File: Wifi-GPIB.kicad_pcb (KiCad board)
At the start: 2 copper layers, 63 x 100.6 mm, 61 parts, among them CON1 POWER_BARREL, P1 CONN_6, P2 CONN_2, P3 CONN_8, P4 GPIB_MALE, P5 CONN_4, Q1 IRLML2246TR, SW1 SW_RESET, SW2 SW_BOOTL, U1 MICRO-B_USB, U2 AP1117E50G-13, U3 LM358, U4 BA33BC0FP-E2, U5 STM32F072CBT6, U6 SN75160B, U7 SN75162B, U8 ESP-12/07v2/08v2

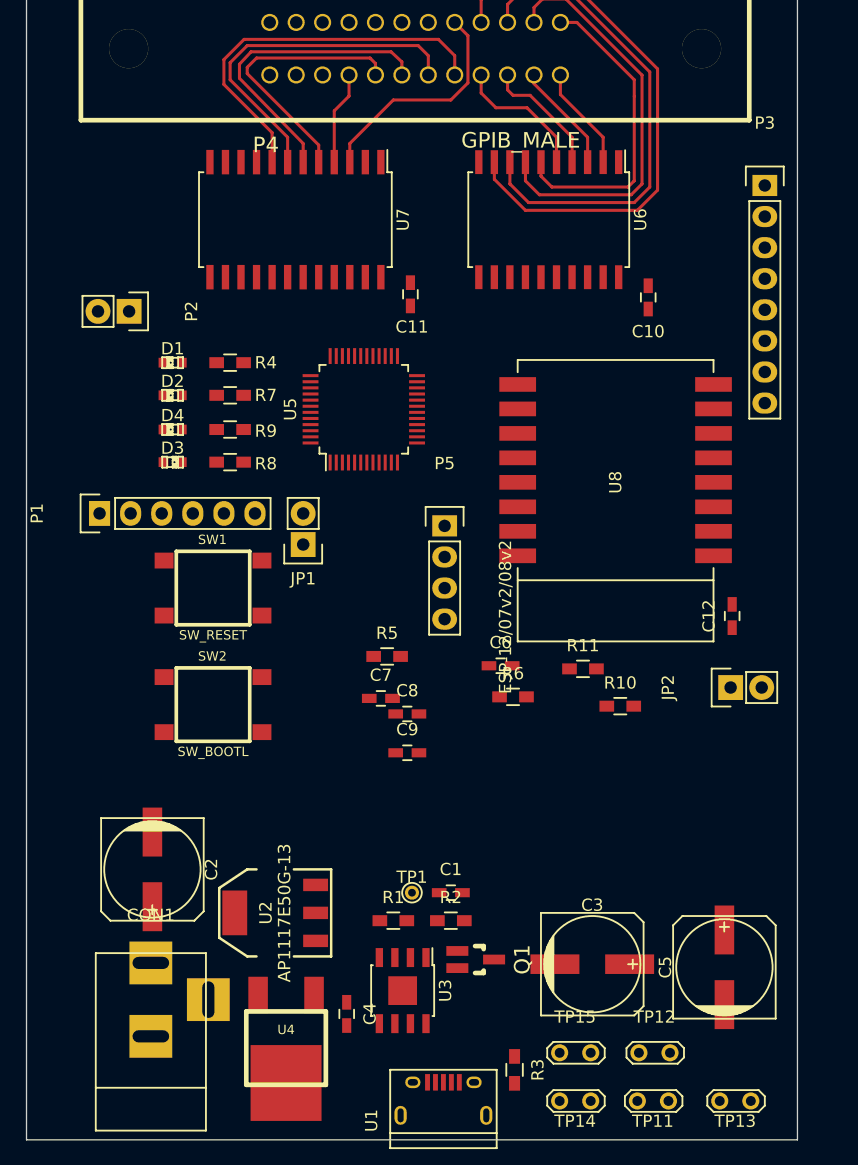
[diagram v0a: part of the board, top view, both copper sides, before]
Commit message: Need to swap gpib line driver buses on stm32
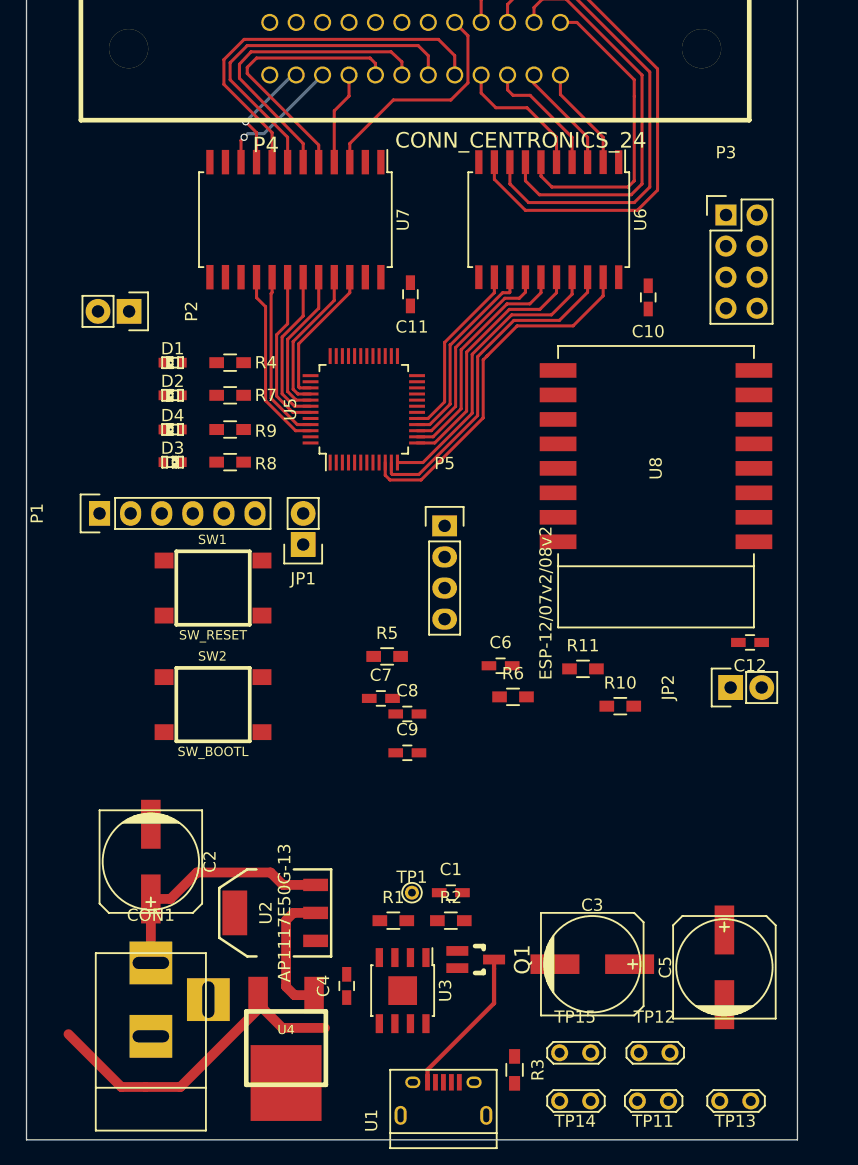
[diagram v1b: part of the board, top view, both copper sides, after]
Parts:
- D1: value POWER -> LED_POWER
- D2: value WIFI -> WIFI_CONNECTED_LED
- D3: value USB -> USB ACTIVITY LED
- D4: value GPIB -> GPIB_SEND
- P3: value CONN_8 -> CONN_4X2; footprint Pin_Headers:Pin_Header_Straight_1x08 -> Pin_Headers:Pin_Header_Straight_2x04
- P4: value GPIB_MALE -> CONN_CENTRONICS_24
- TP11: value 3V3 -> TESTPOINT
- TP12: value VIN -> TESTPOINT
- TP13: value 5V -> TESTPOINT
- TP14, TP15: value GND -> TESTPOINT
- moved P3 3.99 mm to (119.8, 53.1)
- moved U8 3.49 mm to (114.0, 73.8)
- moved C12 2.61 mm to (121.7, 88.0), turned to 180 degrees
- moved C4 2.29 mm to (88.8, 116.1), turned to 90 degrees
- moved C2 0.65 mm to (72.8, 105.9)
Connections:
- P3 pad 2: /GPIB and Cortex M0/ESP_GPIO_4 -> +3.3V
- P3 pad 3: /GPIB and Cortex M0/ESP_GPIO_5 -> /GPIB and Cortex M0/ESP_GPIO_4
- P3 pad 4: /GPIB and Cortex M0/ESP_GPIO_12 -> /GPIB and Cortex M0/ESP_GPIO_15
- P3 pad 5: /GPIB and Cortex M0/ESP_GPIO_13 -> /GPIB and Cortex M0/ESP_GPIO_5
- P3 pad 7: /GPIB and Cortex M0/ESP_GPIO_15 -> /GPIB and Cortex M0/ESP_GPIO_12
- P3 pad 8: +3.3V -> /GPIB and Cortex M0/ESP_GPIO_13
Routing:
- net Net-(U5-Pad10): track 0.00 -> 29.7 mm
- net +3.3V: track 0.00 -> 28.0 mm
- net Net-(U5-Pad11): track 0.00 -> 27.2 mm
- net Net-(U5-Pad12): track 0.00 -> 24.2 mm
- net Net-(U5-Pad13): track 0.00 -> 20.6 mm
- net VIN: track 0.00 -> 20.0 mm
- net Net-(U5-Pad14): track 0.00 -> 19.1 mm
- net Net-(U5-Pad15): track 0.00 -> 17.6 mm
- net Net-(U5-Pad16): track 0.00 -> 16.1 mm
- net Net-(U5-Pad46): track 0.00 -> 15.1 mm
- net Net-(U5-Pad17): track 0.00 -> 14.7 mm
- net Net-(U5-Pad45): track 0.00 -> 14.0 mm
- net Net-(U5-Pad43): track 0.00 -> 13.4 mm
- net Net-(U5-Pad42): track 0.00 -> 13.0 mm
- net Net-(U5-Pad41): track 0.00 -> 12.6 mm
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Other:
- net class PWR added: clearance 0.2, trace_width 0.5, via_dia 1, via_drill 0.6

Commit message: Remove Barrel Jack and associated power circuits. Unnecessary for now and add a lot of complexity / BOM cost
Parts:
- removed C1: 100n, Capacitors_SMD:C_0603_HandSoldering
- removed C2, C3: 47u, Capacitors_SMD:c_elec_8x6.5
- removed CON1: POWER_BARREL, Connect:BARREL_JACK
- removed Q1: IRLML2246TR, SOT23_Transistor_RevA_03Aug2010:SOT23_Transistor_Handsoldering_RevA_03Aug2010
- removed R1, R2: 10K, Resistors_SMD:R_0603_HandSoldering
- removed TP1, TP2, TP3, TP4, TP5, TP6, TP7, TP8: TESTPOINT, Connect:PINTST
- removed TP12: TESTPOINT, Connect:TESTPOINT
- removed U2: AP1117E50G-13, SOT223:SOT223
- removed U3: LM358, Housings_SOIC:SOIC-8-1EP_3.9x4.9mm_Pitch1.27mm
- D1: value LED_POWER -> PWR
- D2: value WIFI_CONNECTED_LED -> WIFI
- D3: value USB ACTIVITY LED -> USB
- D4: value GPIB_SEND -> GPIB
- JP1: value USB_LED_ENABLE -> USB_LED
- P1: value CONN_6 -> SWD
- P2: value CONN_2 -> USART
- P3: value CONN_4X2 -> ESP_EXPANSION
- P5: value CONN_4 -> ESP_PROG
- moved U1 57.6 mm to (66.9, 73.9), turned to 0 degrees
- moved R3 55.6 mm to (70.9, 77.2), turned to 0 degrees
- moved P1 29.5 mm to (97.9, 74.0), turned to 0 degrees
- moved SW1 12.1 mm to (89.7, 86.0)
- moved JP1 11.7 mm to (78.5, 70.4)
- moved C7 11.4 mm to (99.7, 100.6)
- moved C8 11.4 mm to (101.9, 101.9)
- moved R5 11.4 mm to (100.2, 97.2)
- moved C9 11.4 mm to (101.9, 105.0)
- moved SW2 11.3 mm to (89.1, 94.3)
- moved P2 9.03 mm to (66.8, 53.0), turned to 90 degrees
- moved R4 8.67 mm to (72.5, 59.7)
- moved R7 8.67 mm to (72.5, 62.4)
- moved R8 8.67 mm to (72.5, 67.8)
- moved R9 8.67 mm to (72.5, 65.2)
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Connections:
- U1 pad 1: Net-(Q1-Pad3) -> +5V
- U5 pad 10: Net-(U5-Pad10) -> /GPIB and Cortex M0/REN
- U5 pad 11: Net-(U5-Pad11) -> /GPIB and Cortex M0/IFC
- U5 pad 12: Net-(U5-Pad12) -> /GPIB and Cortex M0/NDAC
- U5 pad 13: Net-(U5-Pad13) -> /GPIB and Cortex M0/NRFD
- U5 pad 14: Net-(U5-Pad14) -> /GPIB and Cortex M0/DAV
- U5 pad 15: Net-(U5-Pad15) -> /GPIB and Cortex M0/EOI
- U5 pad 16: Net-(U5-Pad16) -> /GPIB and Cortex M0/ATN
- U5 pad 17: Net-(U5-Pad17) -> /GPIB and Cortex M0/SRQ
- U5 pad 18: GPIB_DATA_TE -> GPIB_CTRL_DC
- U5 pad 20: GPIB_CTRL_TE -> GPIB_CTRL_SC
- U5 pad 25: Net-(U5-Pad25) -> GPIB_DATA_TE
- U5 pad 26: GPIB_CTRL_DC -> GPIB_DATA_PE
- U5 pad 27: GPIB_CTRL_SC -> Net-(U5-Pad27)
- U5 pad 29: GPIB_DATA_PE -> Net-(U5-Pad29)
- U5 pad 38: Net-(U5-Pad38) -> /GPIB and Cortex M0/D1
- U5 pad 39: Net-(U5-Pad39) -> /GPIB and Cortex M0/D2
- U5 pad 40: Net-(U5-Pad40) -> /GPIB and Cortex M0/D3
- U5 pad 41: Net-(U5-Pad41) -> /GPIB and Cortex M0/D4
- U5 pad 42: Net-(U5-Pad42) -> /GPIB and Cortex M0/D5
- U5 pad 43: Net-(U5-Pad43) -> /GPIB and Cortex M0/D6
- U5 pad 45: Net-(U5-Pad45) -> /GPIB and Cortex M0/D7
- U5 pad 46: Net-(U5-Pad46) -> /GPIB and Cortex M0/D8
- U6 pad 12: Net-(U5-Pad17) -> /GPIB and Cortex M0/D8
- U6 pad 13: Net-(U5-Pad16) -> /GPIB and Cortex M0/D7
- U6 pad 14: Net-(U5-Pad15) -> /GPIB and Cortex M0/D6
- U6 pad 15: Net-(U5-Pad14) -> /GPIB and Cortex M0/D5
- U6 pad 16: Net-(U5-Pad13) -> /GPIB and Cortex M0/D4
- U6 pad 17: Net-(U5-Pad12) -> /GPIB and Cortex M0/D3
- U6 pad 18: Net-(U5-Pad11) -> /GPIB and Cortex M0/D2
- U6 pad 19: Net-(U5-Pad10) -> /GPIB and Cortex M0/D1
- U7 pad 15: Net-(U5-Pad25) -> /GPIB and Cortex M0/SRQ
- U7 pad 16: Net-(U5-Pad46) -> /GPIB and Cortex M0/ATN
- U7 pad 17: Net-(U5-Pad45) -> /GPIB and Cortex M0/EOI
- U7 pad 18: Net-(U5-Pad43) -> /GPIB and Cortex M0/DAV
- U7 pad 19: Net-(U5-Pad42) -> /GPIB and Cortex M0/NRFD
- U7 pad 20: Net-(U5-Pad41) -> /GPIB and Cortex M0/NDAC
- U7 pad 21: Net-(U5-Pad40) -> /GPIB and Cortex M0/IFC
- U7 pad 22: Net-(U5-Pad39) -> /GPIB and Cortex M0/REN
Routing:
- net Net-(U5-Pad10): track 29.7 -> 0.00 mm
- net Net-(U5-Pad11): track 27.2 -> 0.00 mm
- net /GPIB and Cortex M0/ESP_GPIO_4: track 0.00 -> 27.1 mm, vias 0 -> 2
- net /GPIB and Cortex M0/USB_D+: track 0.00 -> 26.7 mm
- net +3.3V: track 28.0 -> 1.86 mm
- net /GPIB and Cortex M0/USB_D-: track 0.00 -> 25.8 mm
- net Net-(U5-Pad12): track 24.2 -> 0.00 mm
- net /GPIB and Cortex M0/ESP_GPIO_5: track 0.00 -> 23.8 mm
- net /GPIB and Cortex M0/D1: track 0.00 -> 22.9 mm
- net /GPIB and Cortex M0/D2: track 0.00 -> 21.7 mm
- net /GPIB and Cortex M0/ESP_GPIO_15: track 0.00 -> 21.3 mm
- net Net-(U5-Pad13): track 20.6 -> 0.00 mm
- net VIN: track 20.0 -> 0.00 mm
- net /GPIB and Cortex M0/D3: track 0.00 -> 19.9 mm
- net Net-(U5-Pad14): track 19.1 -> 0.00 mm
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- added copper zone on F.Cu, net GND

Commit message: Placement pretty much there
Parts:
- removed the C5 at (119.6, 114.6)
- added C1: 47u, Capacitors_SMD:c_elec_5x5.3, F.Cu at (72.9, 75.5)
- added C3: 47u, Capacitors_SMD:c_elec_5x5.3, F.Cu at (84.5, 77.7)
- moved U2 52.8 mm to (79.2, 68.6), turned to 270 degrees
- moved TP2 51.6 mm to (93.5, 81.6)
- moved TP1 50.6 mm to (88.7, 81.6), turned to 0 degrees
- moved C2 48.6 mm to (72.5, 70.3), turned to 180 degrees
- moved TP6 43.5 mm to (101.8, 72.1)
- moved JP2 43.0 mm to (119.7, 48.7)
- moved TP3 41.6 mm to (93.5, 86.2)
- moved TP5 40.6 mm to (101.7, 74.6)
- moved TP4 40.1 mm to (88.5, 86.2)
- moved R8 28.4 mm to (100.8, 66.8), turned to 270 degrees
- moved R9 24.0 mm to (102.7, 66.8), turned to 90 degrees
- moved SW1 20.2 mm to (69.6, 83.9)
- moved JP1 18.3 mm to (70.4, 54.1), turned to 270 degrees
- moved SW2 13.4 mm to (80.6, 83.9)
- moved P2 2.97 mm to (67.9, 50.2)
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- renumbered C12 to C10, C4 to C2, C6 to C4, C7 to C5, C8 to C6, C9 to C7, C10 to C8, C11 to C9, R3 to R1, R4 to R2, R5 to R3, R6 to R4, R7 to R5, R8 to R6, R9 to R7, R10 to R8, R11 to R9, TP11 to TP1, TP13 to TP2, TP14 to TP3, TP15 to TP4, TP9 to TP5, TP10 to TP6, U4 to U2, U5 to U3, U6 to U4, U7 to U5, U8 to U6
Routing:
- net +5V: track 0.00 -> 85.8 mm
- net /GPIB and Cortex M0/ESP_TXD: track 0.00 -> 41.3 mm, vias 0 -> 1
- net /GPIB and Cortex M0/ESP_RXD: track 0.00 -> 40.1 mm, vias 0 -> 1
- net ESP_GPIO0: track 0.00 -> 30.2 mm, vias 0 -> 2
- net NRST: track 0.00 -> 27.1 mm, vias 0 -> 1
- net GPIB_DATA_PE: track 0.00 -> 20.0 mm
- net +3.3V: track 1.86 -> 21.8 mm
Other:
- board size 63 x 100.6 mm -> 63 x 65.7 mm

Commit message: More routing
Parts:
- added GND1: GND, Wire_Pads:SolderWirePad_single_0-4mmDrill, F.Cu at (70.0, 63.8)
- added GND10: GND, Wire_Pads:SolderWirePad_single_0-4mmDrill, F.Cu at (70.0, 61.1)
- added GND11: GND, Wire_Pads:SolderWirePad_single_0-4mmDrill, F.Cu at (47.7, 62.9)
- added GND12: GND, Wire_Pads:SolderWirePad_single_0-4mmDrill, F.Cu at (48.7, 62.9)
- added GND13: GND, Wire_Pads:SolderWirePad_single_0-4mmDrill, F.Cu at (49.7, 62.9)
- added GND14: GND, Wire_Pads:SolderWirePad_single_0-4mmDrill, F.Cu at (50.7, 62.9)
- added GND15: GND, Wire_Pads:SolderWirePad_single_0-4mmDrill, F.Cu at (51.7, 62.9)
- added GND16: GND, Wire_Pads:SolderWirePad_single_0-4mmDrill, F.Cu at (52.7, 62.9)
- added GND17: GND, Wire_Pads:SolderWirePad_single_0-4mmDrill, F.Cu at (53.7, 62.9)
- added GND18: GND, Wire_Pads:SolderWirePad_single_0-4mmDrill, F.Cu at (54.7, 62.9)
- added GND19: GND, Wire_Pads:SolderWirePad_single_0-4mmDrill, F.Cu at (66.3, 63.7)
- added GND2: GND, Wire_Pads:SolderWirePad_single_0-4mmDrill, F.Cu at (48.7, 61.9)
- added GND20: GND, Wire_Pads:SolderWirePad_single_0-4mmDrill, F.Cu at (70.0, 66.6)
- added GND21: GND, Wire_Pads:SolderWirePad_single_0-4mmDrill, F.Cu at (47.7, 63.9)
- added GND22: GND, Wire_Pads:SolderWirePad_single_0-4mmDrill, F.Cu at (48.7, 63.9)
- added GND23: GND, Wire_Pads:SolderWirePad_single_0-4mmDrill, F.Cu at (49.7, 63.9)
- added GND24: GND, Wire_Pads:SolderWirePad_single_0-4mmDrill, F.Cu at (50.7, 63.9)
- added GND25: GND, Wire_Pads:SolderWirePad_single_0-4mmDrill, F.Cu at (51.7, 63.9)
- added GND26: GND, Wire_Pads:SolderWirePad_single_0-4mmDrill, F.Cu at (52.7, 63.9)
- added GND27: GND, Wire_Pads:SolderWirePad_single_0-4mmDrill, F.Cu at (53.7, 63.9)
- added GND28: GND, Wire_Pads:SolderWirePad_single_0-4mmDrill, F.Cu at (54.7, 63.9)
- added GND29: GND, Wire_Pads:SolderWirePad_single_0-4mmDrill, F.Cu at (76.1, 58.6)
- added GND3: GND, Wire_Pads:SolderWirePad_single_0-4mmDrill, F.Cu at (49.7, 61.9)
- added GND30: GND, Wire_Pads:SolderWirePad_single_0-4mmDrill, F.Cu at (66.4, 66.5)
- added GND31: GND, Wire_Pads:SolderWirePad_single_0-4mmDrill, F.Cu at (47.7, 64.9)
- added GND32: GND, Wire_Pads:SolderWirePad_single_0-4mmDrill, F.Cu at (48.7, 64.9)
- added GND33: GND, Wire_Pads:SolderWirePad_single_0-4mmDrill, F.Cu at (49.7, 64.9)
- added GND34: GND, Wire_Pads:SolderWirePad_single_0-4mmDrill, F.Cu at (50.7, 64.9)
- added GND35: GND, Wire_Pads:SolderWirePad_single_0-4mmDrill, F.Cu at (51.7, 64.9)
- added GND36: GND, Wire_Pads:SolderWirePad_single_0-4mmDrill, F.Cu at (52.7, 64.9)
- added GND37: GND, Wire_Pads:SolderWirePad_single_0-4mmDrill, F.Cu at (53.7, 64.9)
- added GND38: GND, Wire_Pads:SolderWirePad_single_0-4mmDrill, F.Cu at (54.7, 64.9)
- added GND39: GND, Wire_Pads:SolderWirePad_single_0-4mmDrill, F.Cu at (76.1, 61.3)
- added GND4: GND, Wire_Pads:SolderWirePad_single_0-4mmDrill, F.Cu at (50.7, 61.9)
- added GND40: GND, Wire_Pads:SolderWirePad_single_0-4mmDrill, F.Cu at (76.1, 59.9)
- added GND41: GND, Wire_Pads:SolderWirePad_single_0-4mmDrill, F.Cu at (76.6, 68.3)
- added GND41: GND, Wire_Pads:SolderWirePad_single_0-4mmDrill, F.Cu at (47.7, 65.9)
- added GND410: GND, Wire_Pads:SolderWirePad_single_0-4mmDrill, F.Cu at (78.0, 65.5)
- added GND411: GND, Wire_Pads:SolderWirePad_single_0-4mmDrill, F.Cu at (79.4, 65.5)
- added GND412: GND, Wire_Pads:SolderWirePad_single_0-4mmDrill, F.Cu at (80.8, 65.5)
- added GND413: GND, Wire_Pads:SolderWirePad_single_0-4mmDrill, F.Cu at (76.6, 64.1)
- added GND414: GND, Wire_Pads:SolderWirePad_single_0-4mmDrill, F.Cu at (78.0, 64.1)
- added GND415: GND, Wire_Pads:SolderWirePad_single_0-4mmDrill, F.Cu at (79.4, 64.1)
- added GND416: GND, Wire_Pads:SolderWirePad_single_0-4mmDrill, F.Cu at (80.8, 64.1)
- added GND417: GND, Wire_Pads:SolderWirePad_single_0-4mmDrill, F.Cu at (76.6, 62.7)
- added GND418: GND, Wire_Pads:SolderWirePad_single_0-4mmDrill, F.Cu at (78.0, 62.7)
- added GND419: GND, Wire_Pads:SolderWirePad_single_0-4mmDrill, F.Cu at (79.4, 62.7)
- added GND42: GND, Wire_Pads:SolderWirePad_single_0-4mmDrill, F.Cu at (78.0, 68.3)
- added GND42: GND, Wire_Pads:SolderWirePad_single_0-4mmDrill, F.Cu at (48.7, 65.9)
- added GND420: GND, Wire_Pads:SolderWirePad_single_0-4mmDrill, F.Cu at (80.8, 62.7)
- added GND43: GND, Wire_Pads:SolderWirePad_single_0-4mmDrill, F.Cu at (79.4, 68.3)
- added GND43: GND, Wire_Pads:SolderWirePad_single_0-4mmDrill, F.Cu at (49.7, 65.9)
- added GND44: GND, Wire_Pads:SolderWirePad_single_0-4mmDrill, F.Cu at (80.8, 68.3)
- added GND44: GND, Wire_Pads:SolderWirePad_single_0-4mmDrill, F.Cu at (50.7, 65.9)
- added GND45: GND, Wire_Pads:SolderWirePad_single_0-4mmDrill, F.Cu at (76.6, 66.9)
- added GND45: GND, Wire_Pads:SolderWirePad_single_0-4mmDrill, F.Cu at (51.7, 65.9)
- added GND46: GND, Wire_Pads:SolderWirePad_single_0-4mmDrill, F.Cu at (78.0, 66.9)
- added GND46: GND, Wire_Pads:SolderWirePad_single_0-4mmDrill, F.Cu at (52.7, 65.9)
- added GND47: GND, Wire_Pads:SolderWirePad_single_0-4mmDrill, F.Cu at (79.4, 66.9)
- added GND47: GND, Wire_Pads:SolderWirePad_single_0-4mmDrill, F.Cu at (53.7, 65.9)
- added GND48: GND, Wire_Pads:SolderWirePad_single_0-4mmDrill, F.Cu at (80.8, 66.9)
- added GND48: GND, Wire_Pads:SolderWirePad_single_0-4mmDrill, F.Cu at (54.7, 65.9)
- added GND49: GND, Wire_Pads:SolderWirePad_single_0-4mmDrill, F.Cu at (76.6, 65.5)
- added GND5: GND, Wire_Pads:SolderWirePad_single_0-4mmDrill, F.Cu at (51.7, 61.9)
- added GND50: GND, Wire_Pads:SolderWirePad_single_0-4mmDrill, F.Cu at (70.6, 71.8)
- added GND6: GND, Wire_Pads:SolderWirePad_single_0-4mmDrill, F.Cu at (52.7, 61.9)
- added GND7: GND, Wire_Pads:SolderWirePad_single_0-4mmDrill, F.Cu at (53.7, 61.9)
- added GND8: GND, Wire_Pads:SolderWirePad_single_0-4mmDrill, F.Cu at (54.7, 61.9)
- added GND9: GND, Wire_Pads:SolderWirePad_single_0-4mmDrill, F.Cu at (66.4, 61.0)
- moved TP4 38.3 mm to (95.5, 48.6)
- moved C7 35.9 mm to (77.7, 78.5)
- moved C5 35.4 mm to (66.5, 88.3)
- moved TP2 35.4 mm to (73.9, 52.2), turned to 270 degrees
- moved C4 31.0 mm to (90.9, 60.8), turned to 180 degrees
- moved R3 29.1 mm to (72.5, 88.3)
- moved C6 26.7 mm to (89.3, 78.3), turned to 270 degrees
- moved R4 17.9 mm to (88.1, 81.7), turned to 180 degrees
- moved C9 5.48 mm to (95.6, 54.3)
- moved TP1 4.85 mm to (93.5, 81.8)
- moved P2 0.76 mm to (67.8, 49.4)
- moved U2 0.20 mm to (79.0, 68.6)
- turned C10 to 0 degrees
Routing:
- net +3.3V: track 21.8 -> 176.7 mm, vias 0 -> 6
- net /GPIB and Cortex M0/ESP_GPIO_16: track 0.00 -> 71.1 mm, vias 0 -> 4
- net NRST: track 27.1 -> 96.9 mm, vias 1 -> 7
- net BOOT0: track 0.00 -> 29.8 mm, vias 0 -> 2
- net GPIB_CTRL_SC: track 0.00 -> 25.8 mm, vias 0 -> 2
- net GPIB_CTRL_TE: track 0.00 -> 24.6 mm, vias 0 -> 2
- net GPIB_SEND_LED: track 0.00 -> 21.9 mm, vias 0 -> 2
- net USB_NOE: track 0.00 -> 17.5 mm, vias 0 -> 1
- net GPIB_CTRL_DC: track 0.00 -> 17.2 mm
- net ESP_GPIO0: track 30.2 -> 39.9 mm, vias 2 -> 4
- net GND: track 0.00 -> 8.70 mm, vias 0 -> 1
- net +5V: track 85.8 -> 91.8 mm
- net Net-(C4-Pad1): track 0.00 -> 4.28 mm
- net /GPIB and Cortex M0/ESP_GPIO_15: track 21.3 -> 24.7 mm
- net /GPIB and Cortex M0/ESP_TXD: track 41.3 -> 38.2 mm
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- added copper zone on B.Cu, net GND
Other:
- net class Default: clearance 0.2 -> 0.15
- rule trace_clearance: 0.2 -> 0.15
